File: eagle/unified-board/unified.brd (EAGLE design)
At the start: 76.2 x 50.8 mm, 78 parts, among them IC101 THAT151x, J103 phantom, J104 eqout, J601 out2, U101 OPAMPLME49710, U602 LM3915N, U603 OPAMPLME49710

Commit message: Some initial routing
one input, one output, placeholders  for more.
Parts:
- removed C1, C2: 1uf, SparkFun-Capacitors:CPOL-RADIAL-10UF-25V
- removed C3: 100pf, SparkFun-Capacitors:CAP-PTH-SMALL
- removed D1: RECTIFIERRB15X, mixer:SM-RECTIFIER
- removed FB1: FB, mixer:BEAD
- removed R1, R2: ???, SparkFun-Resistors:AXIAL-0.3
- removed U603: OPAMPLME49710, mixer:DIP08-KIT
- added C604, C606: 1uf, SparkFun-Capacitors:CPOL-RADIAL-10UF-25V
- added C605, C607: 0.01uf, mixer:WIMA-MKS2-2.5X7.2
- added D601: RED, SparkFun-LED:LED_BARGRAPH_10
- added FB601: FB, mixer:BEAD
- added R607, R608, R611: 10k, SparkFun-Resistors:AXIAL-0.3
- added R609: 100, SparkFun-Resistors:AXIAL-0.3
- added R610: 47k, SparkFun-Resistors:AXIAL-0.3
- added U601: LM3915N, SparkFun-IC-Special-Function:DIL18
- C101, C102: value 47p -> 0.01uf; device SparkFun-Capacitors:CAP-PTH-SMALL -> mixer:WIMA-MKS2-2.5X7.2
- C103: value 470p -> 0.015uf; device SparkFun-Capacitors:CAP-PTH-SMALL -> mixer:WIMA-MKS2-2.5X7.2
- C104, C113: value 470p -> 0.1uf; device SparkFun-Capacitors:CAP-PTH-SMALL -> mixer:WIMA-MKS2-2.5X7.2
- C105: value 470p -> 22u; device SparkFun-Capacitors:CAP-PTH-SMALL -> SparkFun-Capacitors:CPOL-RADIAL-100UF-25V
- C107: value 22u -> 470p; device SparkFun-Capacitors:CPOL-RADIAL-100UF-25V -> SparkFun-Capacitors:CAP-PTH-SMALL
- C108, C120: value 22u -> 47p; device SparkFun-Capacitors:CPOL-RADIAL-100UF-25V -> SparkFun-Capacitors:CAP-PTH-SMALL
- C110: value 22u -> 100pf; device SparkFun-Capacitors:CPOL-RADIAL-100UF-25V -> SparkFun-Capacitors:CAP-PTH-SMALL
- C111: value 22u -> 0.015uf; device SparkFun-Capacitors:CPOL-RADIAL-100UF-25V -> mixer:WIMA-MKS2-2.5X7.2
- C115: value 0.1uf -> 22u; device mixer:WIMA-MKS2-2.5X7.2 -> SparkFun-Capacitors:CPOL-RADIAL-100UF-25V
- C116: value 0.1uf -> 470p; device mixer:WIMA-MKS2-2.5X7.2 -> SparkFun-Capacitors:CAP-PTH-SMALL
- C117, C118: value 0.015uf -> 22u; device mixer:WIMA-MKS2-2.5X7.2 -> SparkFun-Capacitors:CPOL-RADIAL-100UF-25V
- C119: value 100pf -> 470p
- C121: value 0.01uf -> 470p; device mixer:WIMA-MKS2-2.5X7.2 -> SparkFun-Capacitors:CAP-PTH-SMALL
- C122: value 0.01uf -> 22u; device mixer:WIMA-MKS2-2.5X7.2 -> SparkFun-Capacitors:CPOL-RADIAL-100UF-25V
- C601, C603: value 0.01uf -> 100pf; device mixer:WIMA-MKS2-2.5X7.2 -> SparkFun-Capacitors:CAP-PTH-SMALL
- D602: value RED -> RECTIFIERRB15X; device SparkFun-LED:LED_BARGRAPH_10 -> mixer:SM-RECTIFIER
- J101: value (none) -> phantom; device SparkFun-Connectors:1X03_NO_SILK -> SparkFun-Connectors:1X01NS-KIT
- J103: value phantom -> eqout
- J104: value eqout -> (none); device SparkFun-Connectors:1X01NS-KIT -> SparkFun-Connectors:1X03_NO_SILK
- R101: value 6k8 -> 1k8
- R102: value 6k8 -> 1k
- R103: value 10 -> 6k8
- R105: value 4k99 -> 1k
- R106: value 4k99 -> 1k2
- R107: value 22k -> 12k
- R108: value 1k2 -> 6k8
- R111: value 1k8 -> 10
- R113: value 12k -> 1k
- R114: value 1k -> 22k
- R115, R116: value 1k -> 4k99
- R601, R602, R603: value 10k -> ???
- U602: value LM3915N -> OPAMPLME49710; device SparkFun-IC-Special-Function:DIL18 -> mixer:DIP08-KIT
- VR101: device mixer:ROT-SW-POT -> mixer:ALPHA-RV24AF40-POT
- VR103: device mixer:ALPHA-RV24AF40-POT -> mixer:ROT-SW-POT
- moved D602 653.3 mm to (157.5, 48.3), turned to 90 degrees
- moved R603 587.4 mm to (144.8, 81.3), turned to 90 degrees
- moved R602 581.1 mm to (147.3, 91.4), turned to 90 degrees
- moved U602 580.6 mm to (162.6, 25.4)
- moved FRAME501 575.5 mm to (86.4, -48.3)
- moved FRAME401 567.4 mm to (86.4, -48.3)
- moved FRAME301 559.3 mm to (86.4, -48.3)
- moved R605 558.7 mm to (165.1, 15.2), turned to 180 degrees
- moved R601 556.3 mm to (147.3, 81.3), turned to 270 degrees
- moved FRAME201 551.2 mm to (86.4, -48.3)
- moved C601 504.9 mm to (167.6, 33.0), turned to 180 degrees
- moved C603 499.2 mm to (157.5, 66.0), turned to 180 degrees
- moved C120 498.0 mm to (20.3, 96.5), turned to 270 degrees
- moved C602 491.7 mm to (157.5, 40.6), turned to 270 degrees
- moved J601 483.6 mm to (160.0, 66.0)
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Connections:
- new net N$12: C602.1, R605.P$1, R609.P$1
- new net N$53: R601.P$1, U601.6
- net 1TO2: now also R604.P$2; no longer R601.P$2
- net 2TO2: now also R606.P$2; no longer R602.P$2
- net 3TO2: now also R607.P$2; no longer R603.P$2
- net 4TO2: now also R608.P$2; no longer R605.P$2
- net GND: now also C101.P$2, C102.P$1, C106.2, C116.2, C603.2, C604.2, C605.P$2, C606.1, C607.P$1, R114.P$2, R602.P$2, R610.P$2, R611.P$1, U601.2, U601.4; no longer C1.1, C112.2, C113.2, C121.P$2, C122.P$1, C2.2, C3.2, C601.P$2, C603.P$1, R107.P$2, R2.P$2, R606.P$1, U602.2
- net N$1: now also C104.P$1, R101.P$1; no longer C115.P$1, R111.P$1
- net N$10: now also C111.P$1, VR101.CW; no longer C118.P$1, VR103.CW
- net N$11: now also D602.AC1, D602.AC2, FB601.P$1, R610.P$1, U601.5; no longer D1.AC1, D1.AC2, FB1.P$1, U602.5
- net N$13: now also R611.P$2, U602.3; no longer R606.P$2, U603.3
- net N$14: now also C104.P$2, C113.P$2, R107.P$2; no longer C115.P$2, C116.P$2, R113.P$2
- net N$15: now also C103.P$2, VR101.CCW; no longer C117.P$2, VR103.CCW
- net N$16: now also C601.2, R609.P$2, U602.6; no longer C602.1, R604.P$1, U603.6
- net N$17: now also C601.1, R604.P$1, R605.P$2, R606.P$1, R607.P$1, R608.P$1, U602.2; no longer R601.P$1, R602.P$1, R603.P$1, R604.P$2, R605.P$1, U603.2
- net N$19: now also C103.P$1, R102.P$1; no longer C117.P$1, R115.P$1
- net N$2: now also C113.P$1; no longer C116.P$1
- net N$20: now also D601.11, U601.1; no longer D602.11, U602.1
- net N$21: now also C115.2; no longer C111.2
- net N$22: now also C109.1; no longer C114.1
- net N$23: now also C108.1, J102.2; no longer C101.1, J101.2
- net N$24: now also C107.2, C108.2, C112.1; no longer C101.2, C103.2, C104.1
- net N$25: now also C105.1, J102.3, R103.P$1; no longer C103.1, J101.3, R101.P$1
- net N$26: now also C112.2, C114.1, J102.1, R108.P$1; no longer C104.2, C108.1, J101.1, R102.P$1
- net N$27: now also C114.2, R111.P$2; no longer C108.2, R104.P$2
- net N$28: now also J101.1, R103.P$2, R108.P$2; no longer J103.1, R101.P$2, R102.P$2
- net N$29: now also C105.2, R104.P$2; no longer C107.2, R103.P$2
- net N$3: now also C110.1, R105.P$2, R107.P$1; no longer C119.1, R113.P$1, R114.P$2
- net N$30: now also R104.P$1, R106.P$1, R115.P$1; no longer R103.P$1, R105.P$1, R108.P$1
- net N$31: now also R111.P$1, R116.P$1; no longer R104.P$1, R106.P$1
- net N$32: now also R106.P$2, R114.P$1; no longer R107.P$1, R108.P$2
- net N$33: now also VR103.CCW, VR103.WIP; no longer VR101.CCW, VR101.WIP
- net N$34: now also VR103.CW; no longer VR101.CW
- net N$35: now also C115.1; no longer C111.1
- net N$36: now also C120.1, J104.2; no longer C102.1, J102.2
- net N$37: now also C119.2, C120.2, C121.1; no longer C102.2, C105.2, C106.1
- net N$38: now also C117.1, C119.1, J104.3; no longer C105.1, C109.1, J102.3
- net N$39: now also C121.2, C122.1, J104.1; no longer C106.2, C110.1, J102.1
- net N$4: now also C111.P$2, R113.P$2; no longer C118.P$2, R116.P$2
- net N$40: now also C122.2, R116.P$2; no longer C110.2, R106.P$2
- net N$41: now also D601.12, U601.18; no longer D602.12, U602.18
- net N$42: now also C117.2, R115.P$2; no longer C109.2, R105.P$2
- net N$43: now also D601.13, U601.17; no longer D602.13, U602.17
- net N$44: now also D601.14, U601.16; no longer D602.14, U602.16
- net N$45: now also D601.15, U601.15; no longer D602.15, U602.15
- net N$46: now also D601.16, U601.14; no longer D602.16, U602.14
- net N$47: now also D601.17, U601.13; no longer D602.17, U602.13
- net N$48: now also D601.18, U601.12; no longer D602.18, U602.12
- net N$49: now also D601.19, U601.11; no longer D602.19, U602.11
- net N$5: now also C118.2, J103.1; no longer C120.2, J104.1
- net N$50: now also D601.20, U601.10; no longer D602.20, U602.10
- net N$51: now also R601.P$2, R603.P$1, U601.7; no longer R1.P$1, U602.6, U602.7
- net N$52: now also R602.P$1, R603.P$2, U601.8; no longer R1.P$2, R2.P$1, U602.8
- net N$6: now also C110.2, C118.1, R101.P$2, R102.P$2; no longer C119.2, C120.1, R111.P$2, R115.P$2
- net N$7: now also C603.1, FB601.P$2; no longer C3.1, FB1.P$2
- net N$8: now also R105.P$1, VR101.WIP; no longer R114.P$1, VR103.WIP
- net N$9: now also C109.2, R113.P$1; no longer C114.2, R116.P$1
- net VCC: now also C101.P$1, C106.1, C604.1, C605.P$1, D601.1, D601.10, D601.2, D601.3, D601.4, D601.5, D601.6, D601.7, D601.8, D601.9, D602.POS, U601.3, U602.7; no longer C112.1, C121.P$1, C2.1, C601.P$1, D1.POS, D602.1, D602.10, D602.2, D602.3, D602.4, D602.5, D602.6, D602.7, D602.8, D602.9, U602.3, U603.7
- net VNEG: now also C102.P$2, C116.1, C606.2, C607.P$2, D602.NEG, U602.4; no longer C1.2, C113.1, C122.P$2, C603.P$2, D1.NEG, U603.4
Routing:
- added copper zone on layer 1, net GND
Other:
- board size 76.2 x 50.8 mm -> 203.2 x 101.6 mm

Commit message: A few tweaks.
Forgot that it needs to run right-to-left.
Added standoffs and some silk legending.
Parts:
- added H1, H10, H11, H12, H2, H3, H4, H5, H6, H7, H8, H9: STAND-OFF, SparkFun-Hardware:STAND-OFF
- added J1: eqout, SparkFun-Connectors:1X01NS-KIT
- added J2: (no value), SparkFun-Connectors:1X05_LONGPADS
- J601: device SparkFun-Connectors:1X01NS-KIT -> SparkFun-Connectors:1X02_LOCK_LONGPADS
- U101, U602: value OPAMPLME49710 -> lme49710
- moved C606 174.7 mm to (29.2, 5.08), turned to 90 degrees
- moved R106 174.0 mm to (176.5, 61.0)
- moved R110 174.0 mm to (181.6, 50.8), turned to 180 degrees
- moved C119 170.2 mm to (193.0, 96.5)
- moved C120 170.2 mm to (190.5, 96.5)
- moved C121 170.2 mm to (188.0, 94.0)
- moved J104 170.2 mm to (188.0, 99.1)
- moved R111 168.9 mm to (181.6, 71.1)
- moved R102 168.0 mm to (190.5, 19.1), turned to 270 degrees
- moved J101 167.6 mm to (185.5, 86.3)
- moved R103 166.4 mm to (179.1, 86.4)
- moved R107 166.4 mm to (191.8, 38.1), turned to 180 degrees
- moved C114 166.4 mm to (179.1, 81.3)
- moved C116 166.4 mm to (168.9, 43.2)
- moved C117 166.4 mm to (194.3, 81.3)
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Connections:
- removed net N$5: C118.2, J103.1, VR104.CW, VR105.CW
- new net EQ1OUT: C118.2, J103.1, J2.1
- net 1TO1: now also J2.2; no longer VR104.WIP
- net 1TO2: now also J2.3; no longer VR105.WIP
- net GND: now also J2.4, J2.5, J601.2; no longer VR104.CCW, VR105.CCW
- net N$9: now also J1.1
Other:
- board text added: "1"
- board text added: "2"
- board text added: "3"
- board text added: "4"
- board text added: "M1"
- board text added: "M2"

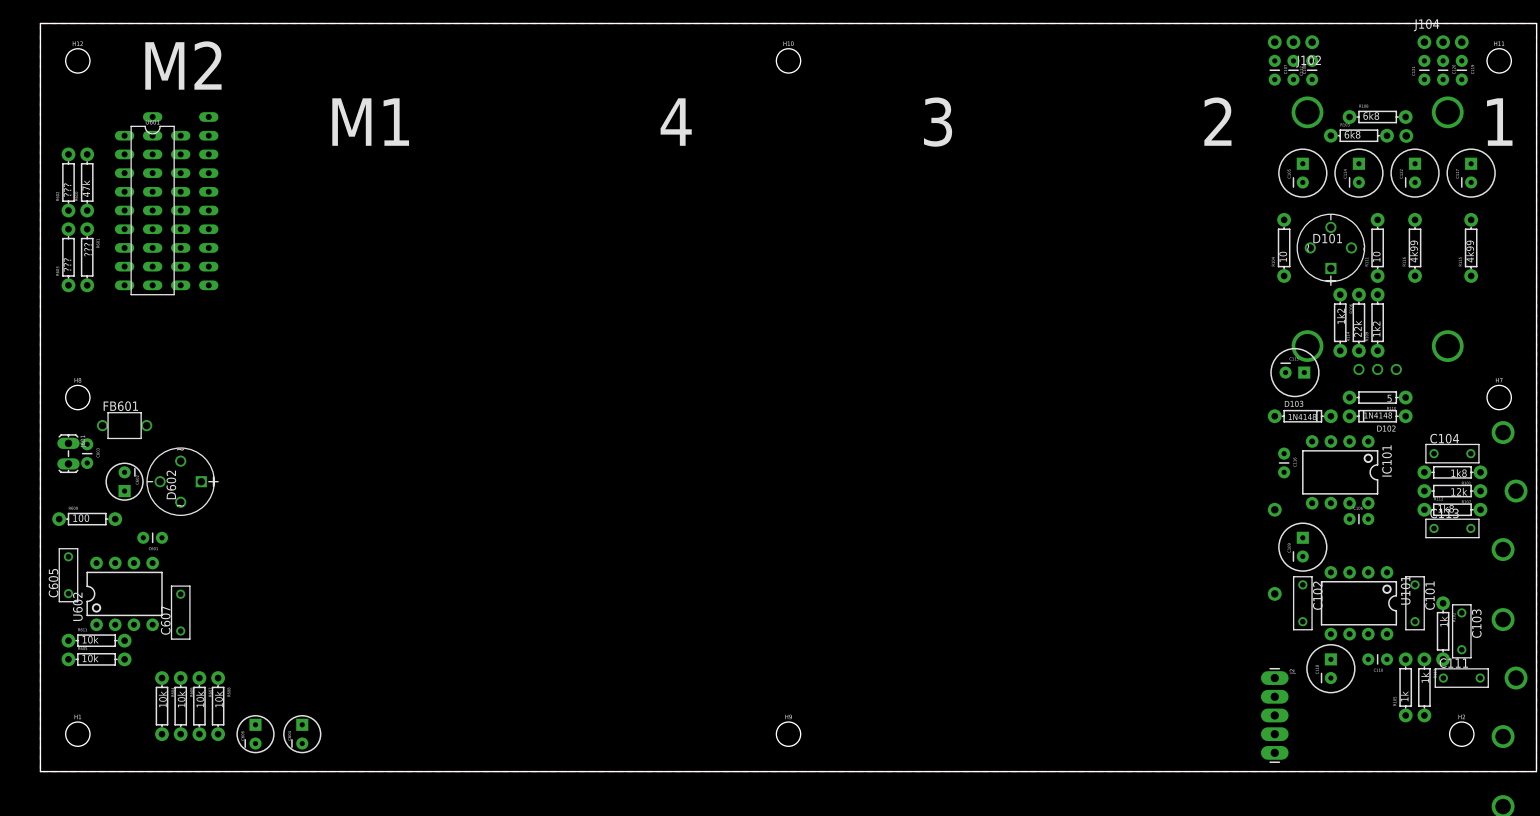
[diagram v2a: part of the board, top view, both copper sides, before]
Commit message: Capacitor update
sourced & created a bunch of caps.
pushed components around more & better.
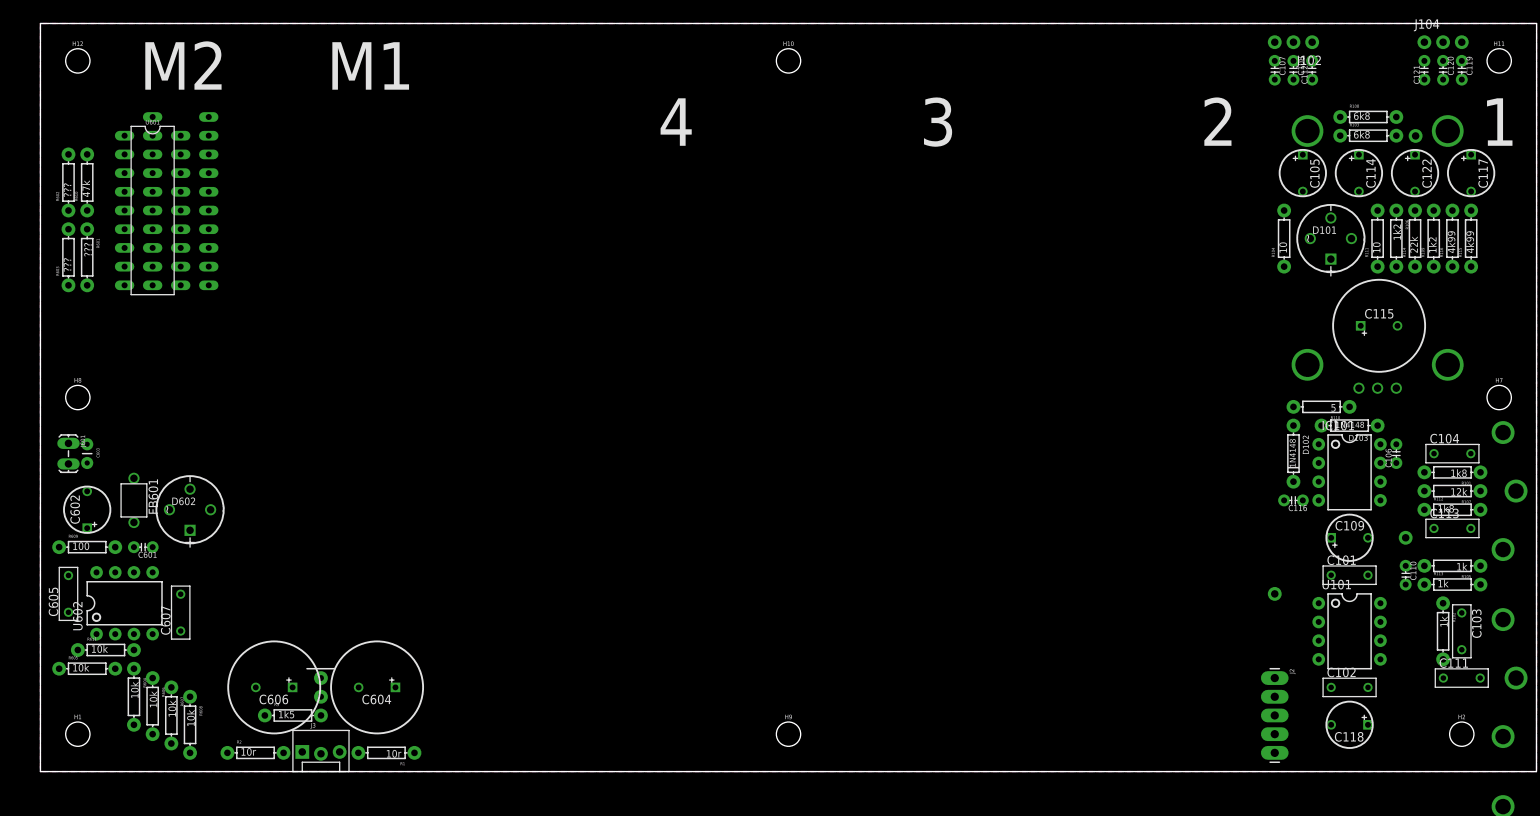
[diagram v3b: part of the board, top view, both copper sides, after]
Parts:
- added D1: (no value), SparkFun-LED:LED_5MM
- added J3: power, SparkFun-Connectors:MOLEX-1X3_LOCK
- added R1, R2: 10r, SparkFun-Resistors:AXIAL-0.3
- added R3: 1k5, SparkFun-Resistors:AXIAL-0.3
- C105, C114: value 22u -> 47u/63V; device SparkFun-Capacitors:CPOL-RADIAL-100UF-25V -> mixer:CAP-PANA-5LS-6DIAM
- C106, C107, C112, C116, C119, C121: value 470p -> 470pf; device SparkFun-Capacitors:CAP-PTH-SMALL -> mixer:CAP-KEMET-GM-2.54LS
- C108, C120: value 47p -> 47pf; device SparkFun-Capacitors:CAP-PTH-SMALL -> mixer:CAP-KEMET-GM-2.54LS
- C109, C117, C118, C122: value 22u -> 47u/25V; device SparkFun-Capacitors:CPOL-RADIAL-100UF-25V -> mixer:CAP-PANA-5LS-5DIAM
- C110, C601: device SparkFun-Capacitors:CAP-PTH-SMALL -> mixer:CAP-KEMET-GM-2.54LS
- C115: value 22u -> 6800u/25V; device SparkFun-Capacitors:CPOL-RADIAL-100UF-25V -> mixer:CAP-PANA-5LS-12.5DIAM
- C602: value 10uf -> 47u/25V; device SparkFun-Capacitors:CPOL-RADIAL-10UF-25V -> mixer:CAP-PANA-5LS-5DIAM
- C604, C606: value 1uf -> 1000u/35V; device SparkFun-Capacitors:CPOL-RADIAL-10UF-25V -> mixer:CAP-PANA-5LS-12.5DIAM
- J102, J104: device SparkFun-Connectors:1X03_NO_SILK -> SparkFun-Connectors:1X03_NO_SILK@1
- moved J1 18.2 mm to (185.4, 31.8), turned to 90 degrees
- moved R105 17.7 mm to (191.8, 27.9), turned to 180 degrees
- moved R113 14.5 mm to (191.8, 25.4), turned to 0 degrees
- moved R106 13.7 mm to (184.2, 72.4)
- moved R114 13.7 mm to (186.7, 72.4)
- moved R109 13.7 mm to (189.2, 72.4)
- moved C102 13.1 mm to (177.8, 11.4), turned to 0 degrees
- moved C115 13.1 mm to (181.8, 60.5)
- moved D102 12.5 mm to (170.2, 43.2), turned to 270 degrees
- moved C604 12.0 mm to (45.7, 11.4), turned to 180 degrees
- moved C110 11.7 mm to (185.4, 26.7), turned to 270 degrees
- moved C106 10.9 mm to (184.2, 43.2), turned to 90 degrees
- moved FB601 10.2 mm to (12.7, 36.8), turned to 270 degrees
- moved C101 9.67 mm to (177.8, 26.7), turned to 0 degrees
- moved C118 8.03 mm to (177.8, 6.35), turned to 180 degrees
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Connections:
- new net N$18: J3.3, R1.P$2
- new net N$5: J3.1, R2.P$2
- new net N$54: D1.A, R3.P$2
- net EQ1OUT: now also C118.NEG; no longer C118.2
- net GND: now also C106.P$2, C116.P$2, C604.NEG, C606.POS, D1.K, J3.2, VR104.CCW, VR105.CCW; no longer C106.2, C116.2, C604.2, C606.1
- net N$11: now also C602.NEG; no longer C602.2
- net N$12: now also C602.POS; no longer C602.1
- net N$16: now also C601.P$2; no longer C601.2
- net N$17: now also C601.P$1; no longer C601.1
- net N$21: now also C115.NEG; no longer C115.2
- net N$22: now also C109.POS; no longer C109.1
- net N$23: now also C108.P$1; no longer C108.1
- net N$24: now also C107.P$2, C108.P$2, C112.P$1; no longer C107.2, C108.2, C112.1
- net N$25: now also C105.POS, C107.P$1; no longer C105.1, C107.1
- net N$26: now also C112.P$2, C114.POS; no longer C112.2, C114.1
- net N$27: now also C114.NEG; no longer C114.2
- net N$29: now also C105.NEG; no longer C105.2
- net N$3: now also C110.P$1; no longer C110.1
- net N$35: now also C115.POS; no longer C115.1
- net N$36: now also C120.P$1; no longer C120.1
- net N$37: now also C119.P$2, C120.P$2, C121.P$1; no longer C119.2, C120.2, C121.1
- net N$38: now also C117.POS, C119.P$1; no longer C117.1, C119.1
- net N$39: now also C121.P$2, C122.POS; no longer C121.2, C122.1
- net N$40: now also C122.NEG; no longer C122.2
- net N$42: now also C117.NEG; no longer C117.2
- net N$6: now also C110.P$2, C118.POS; no longer C110.2, C118.1
- net N$9: now also C109.NEG; no longer C109.2
- net VCC: now also C106.P$1, C604.POS, R1.P$1, R3.P$1; no longer C106.1, C604.1
- net VNEG: now also C116.P$1, C606.NEG, R2.P$1; no longer C116.1, C606.2

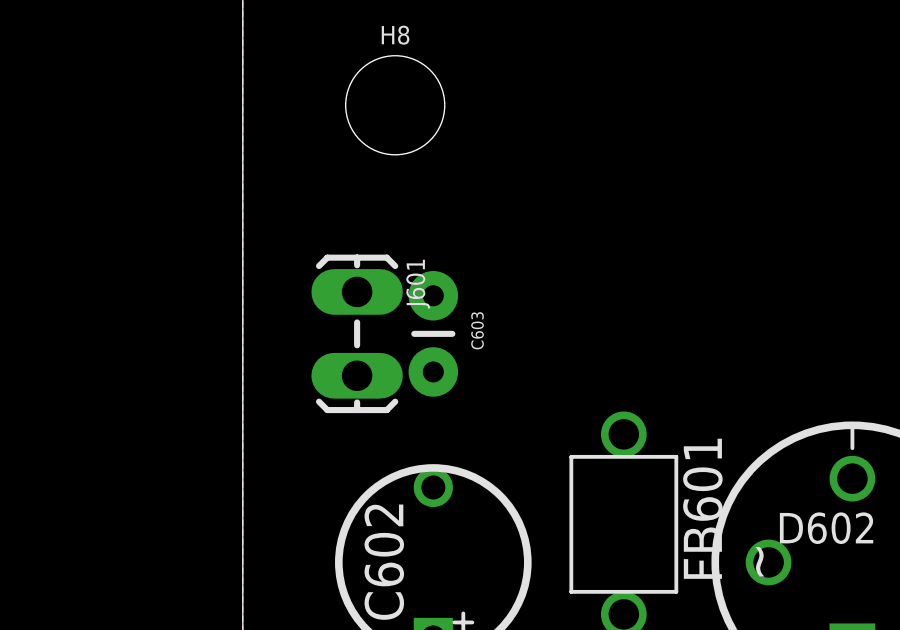
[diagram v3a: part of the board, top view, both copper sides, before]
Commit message: Conforming parts on BOM for ordering.
verified mouser & SFe part #s.
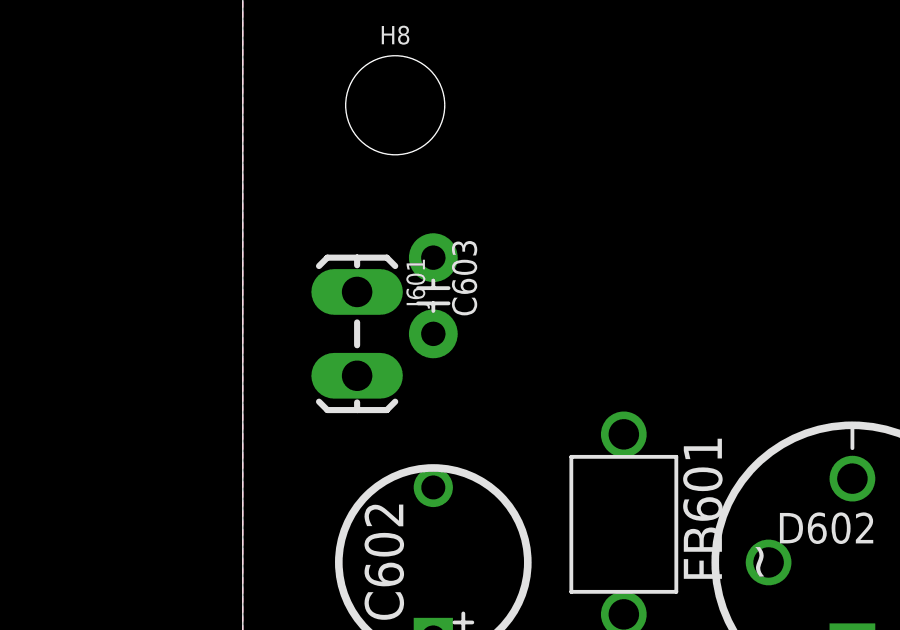
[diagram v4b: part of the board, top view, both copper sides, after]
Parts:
- C603: device SparkFun-Capacitors:CAP-PTH-SMALL -> mixer:CAP-KEMET-GM-2.54LS
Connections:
- net GND: now also C603.P$2; no longer C603.2
- net N$7: now also C603.P$1; no longer C603.1
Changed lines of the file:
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@@
 <attribute name="MOUSER" value="623-2743002112LF" x="12.7" y="36.83" size="1.778" layer="27" font="vector" ratio="15" rot="R270" display="off"/>
 </element>
-<element name="C603" library="SparkFun-Capacitors" package="CAP-PTH-SMALL" value="100pf" x="6.35" y="44.45" rot="R270"/>
+<element name="C603" library="mixer" package="CAP-KEMET-GM-2.54LS" value="100pf" x="6.35" y="44.45" rot="R270">
+<attribute name="MOUSER" value="80-C315C101J5G" x="6.35" y="44.45" size="1.778" layer="27" rot="R270" display="off"/>
+<attribute name="VALUE" value="100pf" x="6.35" y="44.45" size="1.778" layer="27" rot="R270" display="off"/>
+</element>
 <element name="D602" library="mixer" package="SM-RECTIFIER" value="RECTIFIERRB15X" x="20.32" y="35.56">
 <attribute name="MOUSER" value="583-RB153" x="20.32" y="35.56" size="1.778" layer="27" font="vector" ratio="15" display="off"/>
@@
 <contactref element="C604" pad="NEG"/>
 <contactref element="C606" pad="POS"/>
-<contactref element="C603" pad="2"/>
+<contactref element="C603" pad="P$2"/>
 <contactref element="U601" pad="2"/>
 <contactref element="R602" pad="P$2"/>
@@
 <signal name="N$7">
 <contactref element="J601" pad="1"/>
-<contactref element="C603" pad="1"/>
+<contactref element="C603" pad="P$1"/>
 <contactref element="FB601" pad="P$2"/>
-<wire x1="6.35" y1="44.45" x2="12.7" y2="39.83" width="0" layer="19" extent="1-1"/>
-<wire x1="3.81" y1="44.577" x2="6.35" y2="44.45" width="0" layer="19" extent="1-1"/>
+<wire x1="6.35" y1="45.72" x2="12.7" y2="39.83" width="0" layer="19" extent="1-1"/>
+<wire x1="3.81" y1="44.577" x2="6.35" y2="45.72" width="0" layer="19" extent="1-1"/>
 </signal>
 <signal name="N$11">
